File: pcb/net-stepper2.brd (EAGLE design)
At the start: 41.9 x 90.2 mm, 41 parts, among them IC2 CP2104, J1 MICRO-USB, J2 POWER_JACKPTH_LOCK, J3 ENCODER, J4 ENDSTOP2, J5 ENDSTOP1, J6 STEPER, Q1 600mA/40V, Q2 600mA/40V, U1 L6470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

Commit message: moved board
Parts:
- moved U$11 2.84 mm to (39.4, 87.6)
- moved A1 2.84 mm to (7.62, 78.7)
- moved IC2 2.84 mm to (5.84, 68.7)
- moved J1 2.84 mm to (1.40, 77.6)
- moved J5 2.84 mm to (5.08, 41.9)
- moved U$12 2.84 mm to (2.54, 87.6)
- moved U1 2.84 mm to (27.9, 63.5)
- moved U4 2.84 mm to (14.0, 82.5)
- moved C4 2.84 mm to (37.7, 54.9)
- moved S4 2.84 mm to (21.0, 7.62)
- moved U$10 2.84 mm to (39.4, 2.54)
- moved A2 2.84 mm to (2.54, 2.54)
- moved D1 2.84 mm to (32.4, 56.5)
- moved J2 2.84 mm to (45.7, 33.7)
- moved U$9 2.84 mm to (2.54, 2.54)
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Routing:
- net OUT1B: track 42.9 -> 42.3 mm

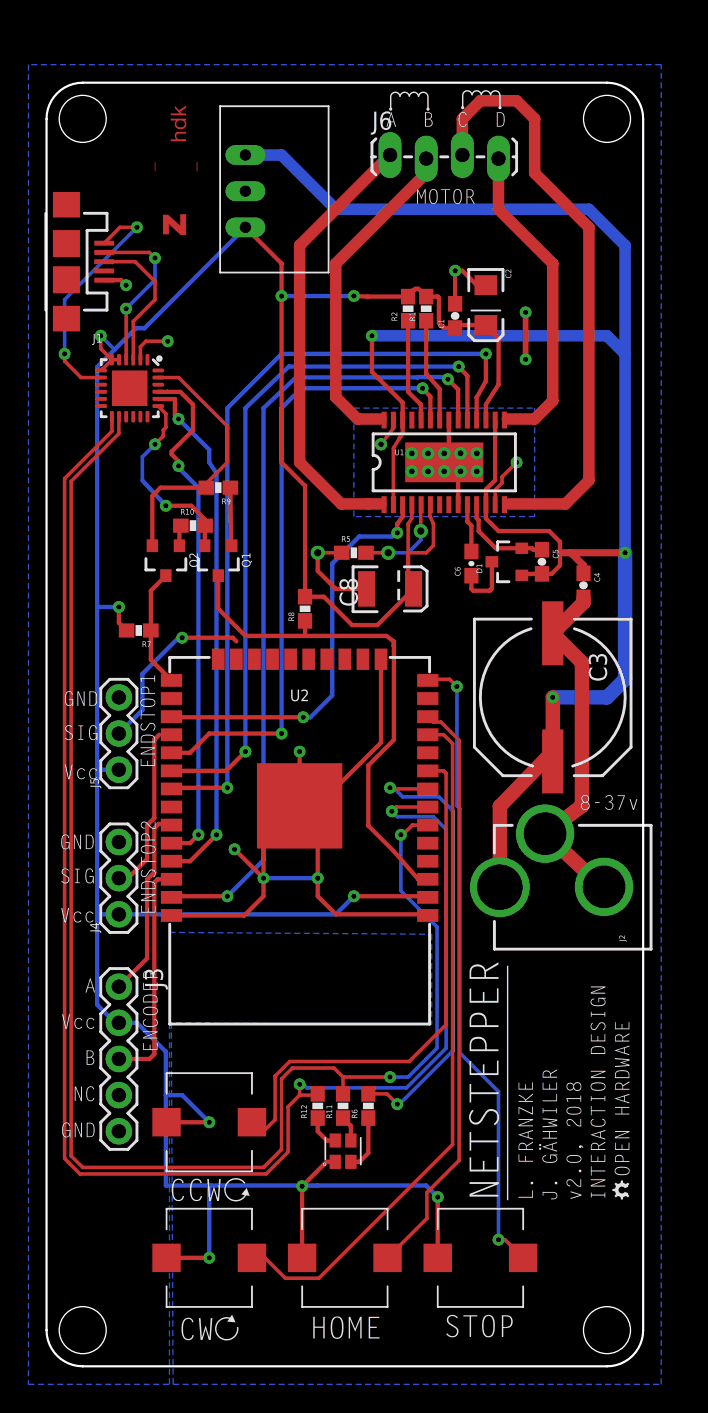
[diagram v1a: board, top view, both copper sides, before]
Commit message: replaced esp32 component
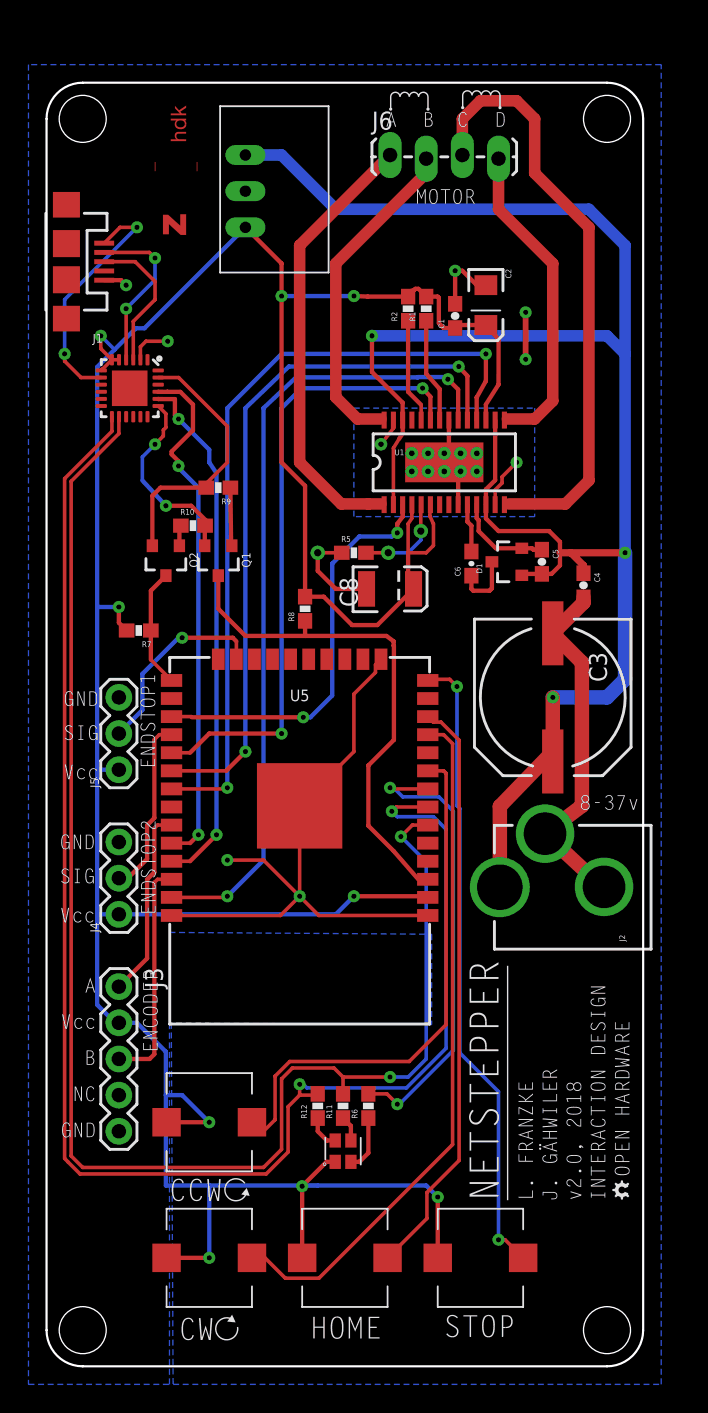
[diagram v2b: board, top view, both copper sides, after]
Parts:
- removed U2: ESP-WROOM-03, esp32:ESP-WROOM-03
- added U5: ESP-WROOM-32, esp32:ESP-WROOM-32
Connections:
- removed net ESTOP1: U2.23
- removed net ESTOP2: U2.28
- removed net N$1: U2.10
- removed net N$10: U2.22
- removed net N$100: U2.16
- removed net N$101: U2.32
- removed net N$2: U2.17
- removed net N$3: U2.18
- removed net N$4: U2.19
- removed net N$5: U2.20
- removed net N$6: U2.21
- removed net N$8: U2.4
- removed net N$9: U2.5
- net 3.3V: now also U5.2; no longer U2.2
- net BLUE: now also U5.7; no longer U2.7
- net CSN: now also U5.29; no longer U2.29
- net DOWN: now also U5.11; no longer U2.11
- net ENC_A: now also U5.33; no longer U2.33
- net ENC_B: now also U5.36; no longer U2.36
- net ENDSTOP1: now also U5.23
- net ENDSTOP2: now also U5.28
- net GND: now also U5.1, U5.15, U5.38, U5.GND; no longer U2.1, U2.15, U2.38, U2.GND
- net GREEN: now also U5.6; no longer U2.6
- net HOME: now also U5.12; no longer U2.12
- net PGRM: now also U5.25; no longer U2.25
- net RED: now also U5.8; no longer U2.8
- net RESET: now also U5.3; no longer U2.3
- net RESETN: now also U5.27; no longer U2.27
- net RX: now also U5.34; no longer U2.34
- net SCK: now also U5.30; no longer U2.30
- net SDI: now also U5.37; no longer U2.37
- net SDO: now also U5.31; no longer U2.31
- net STOP: now also U5.14; no longer U2.14
- net TX: now also U5.35; no longer U2.35
- net UP: now also U5.9; no longer U2.9
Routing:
- net GND: track 104.7 -> 102.1 mm, vias 22 -> 20
- net 3.3V: track 227.9 -> 229.1 mm
- net ENDSTOP1: track 12.6 -> 13.9 mm
- net ENDSTOP2: track 11.7 -> 12.6 mm
- net GREEN: track 105.8 -> 105.0 mm

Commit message: removed unused signals
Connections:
- removed net NC: J3.4
- removed net OSCIN: U1.7
- removed net OSCOUT: U1.8
- removed net STCK: U1.25
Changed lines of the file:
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@@
 <wire x1="26.67" y1="73.445" x2="26.67" y2="73.152" width="0.254" layer="1"/>
-</signal>
-<signal name="STCK">
-<contactref element="U1" pad="25"/>
 </signal>
 <signal name="V_CP">
@@
 <wire x1="5.08" y1="31.75" x2="3.556" y2="31.75" width="0.3048" layer="16"/>
 </signal>
-<signal name="OSCIN">
-<contactref element="U1" pad="7"/>
-</signal>
-<signal name="OSCOUT">
-<contactref element="U1" pad="8"/>
-</signal>
 <signal name="RESETN">
 <contactref element="U1" pad="3"/>
@@
 <wire x1="7.794" y1="34.21" x2="7.5728" y2="33.9888" width="0.254" layer="1"/>
 </signal>
-<signal name="NC">
-<contactref element="J3" pad="4"/>
-</signal>
 <signal name="DOWN">

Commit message: reorganized schematics
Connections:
- net ENDSTOP1 renamed END_STOP_1
- net ENDSTOP2 renamed END_STOP_2
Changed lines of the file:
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@@
 <wire x1="8.78" y1="36.75" x2="10.08" y2="36.75" width="0.254" layer="1"/>
 </signal>
-<signal name="ENDSTOP1">
+<signal name="END_STOP_1">
 <contactref element="J5" pad="2"/>
 <wire x1="13.335" y1="50.927" x2="13.081" y2="51.181" width="0.3048" layer="1"/>
@@
 <wire x1="13.335" y1="49.67" x2="13.335" y2="50.927" width="0.254" layer="1"/>
 </signal>
-<signal name="ENDSTOP2">
+<signal name="END_STOP_2">
 <contactref element="J4" pad="2"/>
 <wire x1="5.16" y1="34.21" x2="5.08" y2="34.29" width="0.3048" layer="1"/>

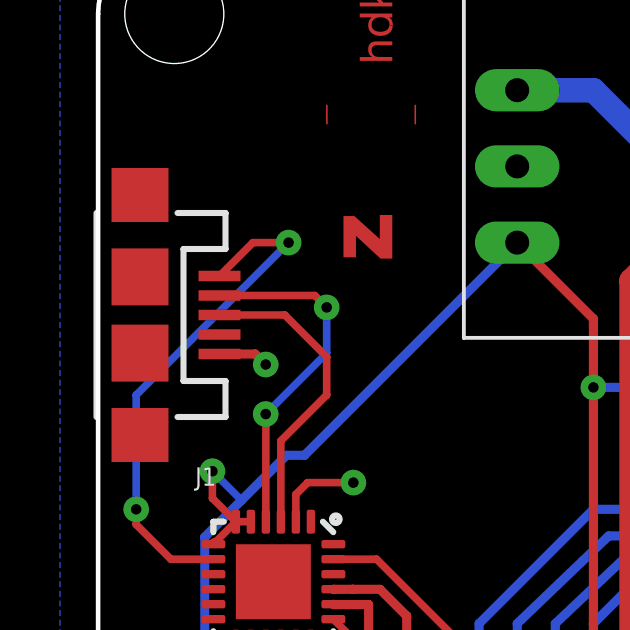
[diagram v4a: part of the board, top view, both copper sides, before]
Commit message: connect usb mounting pins to ground
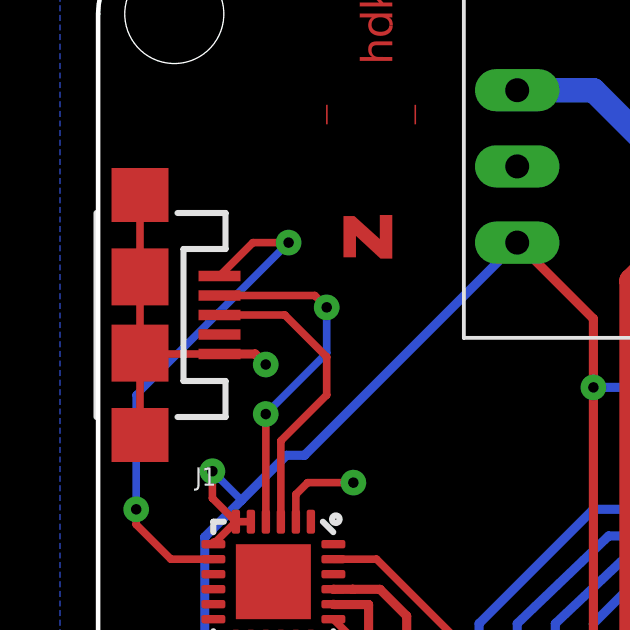
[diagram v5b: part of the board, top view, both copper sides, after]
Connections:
- net GND: now also J1.MT1, J1.MT2, J1.P$1, J1.P$2
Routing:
- net GND: track 102.1 -> 112.7 mm
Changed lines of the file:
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@@
 <wire x1="21.59" y1="43.18" x2="17.78" y2="39.37" width="0.254" layer="1"/>
 <wire x1="21.59" y1="47.22434375" x2="21.59" y2="43.18" width="0.254" layer="1"/>
+<contactref element="J1" pad="P$1"/>
+<contactref element="J1" pad="P$2"/>
+<contactref element="J1" pad="MT1"/>
+<contactref element="J1" pad="MT2"/>
+<wire x1="4.047" y1="76.297" x2="1.427" y2="76.297" width="0.254" layer="1"/>
+<wire x1="1.427" y1="76.297" x2="1.397" y2="76.327" width="0.254" layer="1"/>
+<wire x1="1.397" y1="76.327" x2="1.397" y2="73.597" width="0.254" layer="1"/>
+<wire x1="1.397" y1="76.327" x2="1.397" y2="78.867" width="0.254" layer="1"/>
+<wire x1="1.397" y1="81.597" x2="1.397" y2="78.867" width="0.254" layer="1"/>
 </signal>
 <signal name="FLAGN">

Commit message: changed pull resistors to 10k in order remove one resistor family
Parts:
- R10, R9: value 12k -> 10k
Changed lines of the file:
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@@
 <element name="R7" library="SparkFun-Passives" package="0603-RES" value="10k" x="6.477" y="51.689" rot="R180"/>
 <element name="R8" library="SparkFun-Passives" package="0603-RES" value="10k" x="18.161" y="53.213" rot="R90"/>
-<element name="R9" library="SparkFun-Passives" package="0603-RES" value="12k" x="12.065" y="61.722" rot="R180"/>
-<element name="R10" library="SparkFun-Passives" package="0603-RES" value="12k" x="10.287" y="59.055"/>
+<element name="R9" library="SparkFun-Passives" package="0603-RES" value="10k" x="12.065" y="61.722" rot="R180"/>
+<element name="R10" library="SparkFun-Passives" package="0603-RES" value="10k" x="10.287" y="59.055"/>
 <element name="J3" library="SparkFun-Connectors" package="1X05" value="ENCODER" x="5.08" y="26.67" smashed="yes" rot="R270">
 <attribute name="NAME" x="6.9088" y="28.0162" size="1.27" layer="25" ratio="10" rot="R270"/>

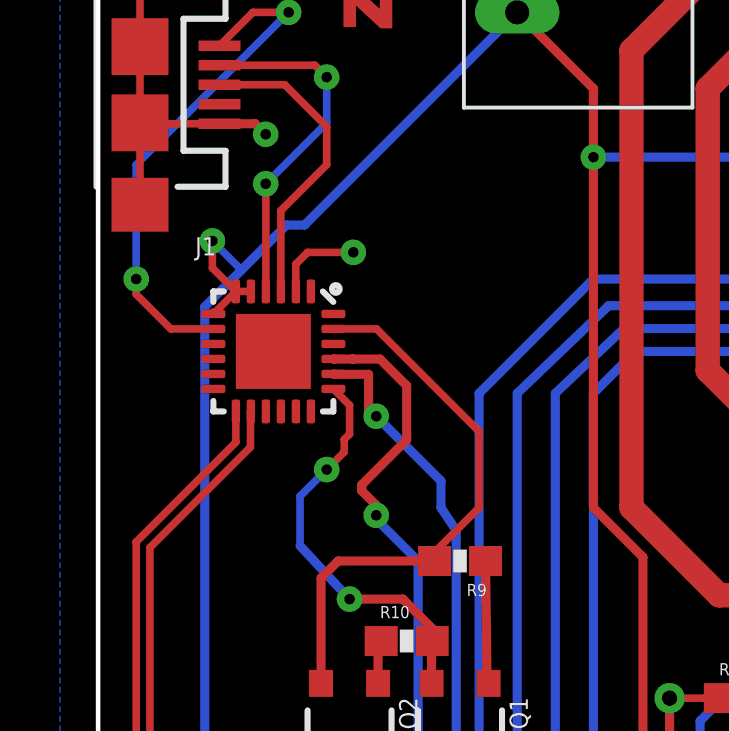
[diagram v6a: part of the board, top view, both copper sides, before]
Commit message: replaced cp2104 in order to connect the thermal pad to ground
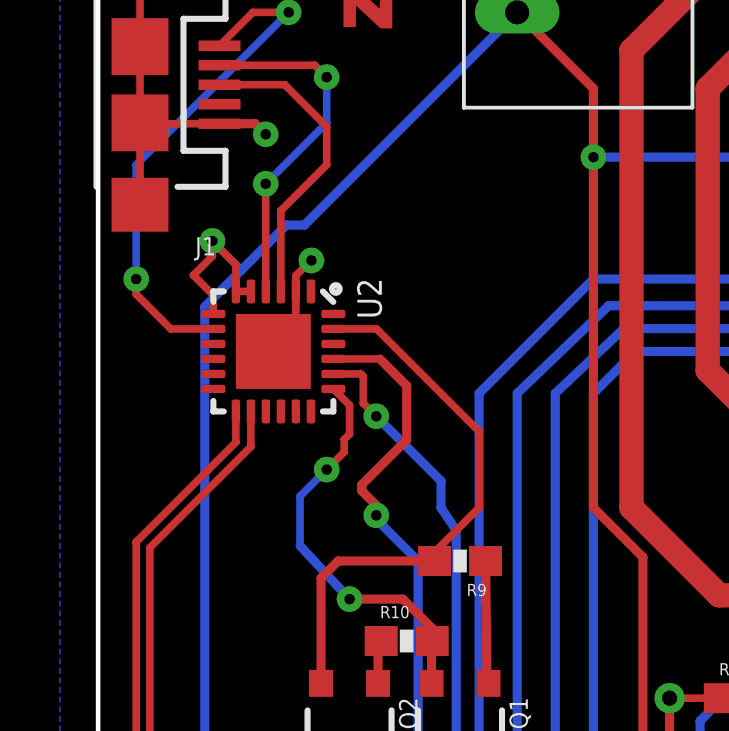
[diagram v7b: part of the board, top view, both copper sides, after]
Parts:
- renumbered IC2 to U2
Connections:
- removed net TP: U2.THERM
- net GND: now also U2.THERM
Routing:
- net 3.3V: track 229.1 -> 231.0 mm
- net GND: track 112.7 -> 113.3 mm

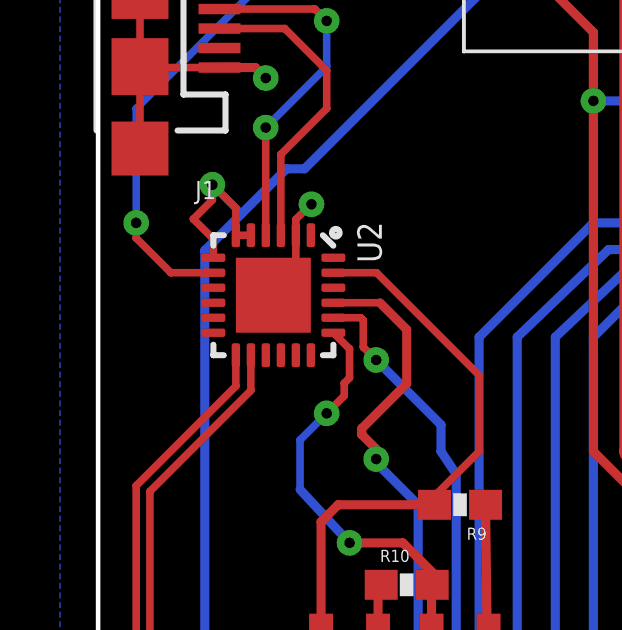
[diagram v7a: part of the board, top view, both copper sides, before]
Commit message: added capacitor
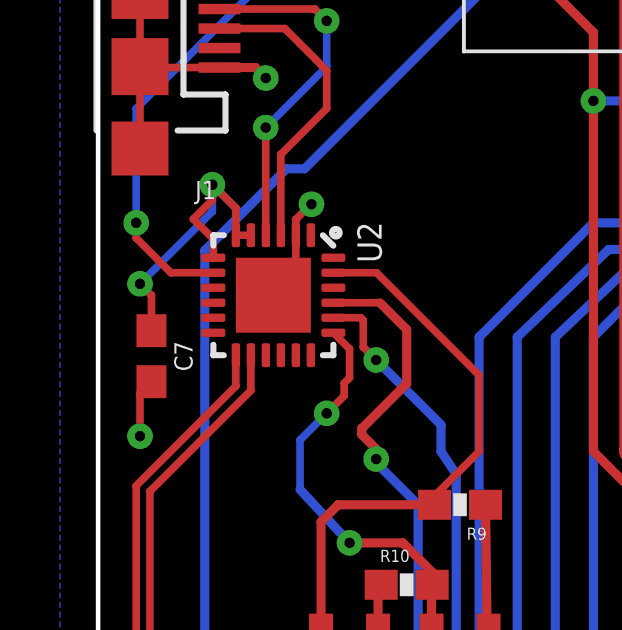
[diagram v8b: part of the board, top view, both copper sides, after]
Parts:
- added C7: 10uF, SparkFun-Capacitors:0603
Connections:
- net 3.3V: now also C7.1
- net GND: now also C7.2
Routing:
- net 3.3V: track 231.0 -> 237.0 mm, vias 9 -> 10
- net GND: track 113.3 -> 115.3 mm, vias 20 -> 21
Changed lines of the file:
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@@
 <element name="U5" library="esp32" package="ESP-WROOM-32" value="ESP-WROOM-32" x="17.78" y="39.37" rot="R270"/>
 <element name="U2" library="microbuilder" package="QFN24_4MM_SMSC" value="CP2104" x="5.842" y="68.707" rot="R270"/>
+<element name="C7" library="SparkFun-Capacitors" package="0603" value="10uF" x="1.778" y="66.675" rot="R270">
+<attribute name="PROD_ID" value="CAP-11015" x="1.778" y="66.675" size="1.778" layer="27" rot="R270" display="off"/>
+</element>
 </elements>
 <signals>
@@
 <wire x1="6.604" y1="69.723" x2="5.842" y2="68.961" width="0.254" layer="1"/>
 <wire x1="5.842" y1="68.961" x2="5.842" y2="68.707" width="0.254" layer="1"/>
+<contactref element="C7" pad="2"/>
+<wire x1="1.778" y1="65.825" x2="1.397" y2="65.444" width="0.254" layer="1"/>
+<wire x1="1.397" y1="65.444" x2="1.397" y2="64.008" width="0.254" layer="1"/>
+<via x="1.397" y="64.008" extent="1-16" drill="0.35"/>
 </signal>
 <signal name="FLAGN">
@@
 <wire x1="3.81" y1="71.882" x2="3.81" y2="72.39" width="0.254" layer="1"/>
 <wire x1="5.092" y1="70.707" x2="4.592" y2="70.707" width="0.254" layer="1"/>
+<contactref element="C7" pad="1"/>
+<wire x1="1.778" y1="67.525" x2="1.778" y2="68.707" width="0.254" layer="1"/>
+<wire x1="1.778" y1="68.707" x2="1.397" y2="69.088" width="0.254" layer="1"/>
+<via x="1.397" y="69.088" extent="1-16" drill="0.35"/>
+<wire x1="1.397" y1="69.088" x2="3.81" y2="71.501" width="0.254" layer="16"/>
+<wire x1="3.81" y1="71.501" x2="3.81" y2="72.39" width="0.254" layer="16"/>
 </signal>
 <signal name="RESETN">
